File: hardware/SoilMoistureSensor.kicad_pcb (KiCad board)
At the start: 2 copper layers, 30 parts, among them Q1 AO3401A, SW1 SW_Push, SW2 SW_Push, U1 BQ25570, U2 ESP32-C3-WROOM-02, U3 TLC555xD

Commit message: started layout in pcb
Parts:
- moved R3 60.9 mm to (172.5, 86.5), turned to 180 degrees
- moved R4 59.0 mm to (170.5, 88.5), turned to 180 degrees
- moved R6 57.9 mm to (174.0, 83.5), turned to -90 degrees
- moved R5 57.6 mm to (168.5, 86.5)
- moved R7 56.0 mm to (172.0, 83.0), turned to 90 degrees
- moved R2 53.8 mm to (165.5, 87.0), turned to 90 degrees
- moved R1 51.8 mm to (163.5, 85.0), turned to 90 degrees
- moved Q1 47.1 mm to (106.9, 84.5)
- moved C9 46.3 mm to (97.0, 62.0), turned to -90 degrees
- moved C1 42.6 mm to (167.0, 55.0)
- moved R12 37.0 mm to (156.5, 78.5)
- moved SW1 34.1 mm to (102.3, 63.1)
- moved C2 33.1 mm to (168.0, 77.0)
- moved SW2 32.7 mm to (102.5, 72.0)
- moved C3 32.5 mm to (168.0, 79.0)
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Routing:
- net /VRDIV: track 0.00 -> 18.9 mm
- net /OK_PROG_N: track 0.00 -> 5.94 mm
- net /VBAT: track 0.00 -> 5.91 mm
- net /VOUT_SET_N: track 0.00 -> 5.09 mm
- net /VBAT_OV_N: track 0.00 -> 4.94 mm
- net /OK_HYST_N: track 0.00 -> 4.63 mm
- net /VSTOR: track 0.00 -> 3.92 mm
- net /VREF_SAMP: track 0.00 -> 3.09 mm
- net GND: track 0.00 -> 2.33 mm

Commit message: continued placing parts in layout
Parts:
- moved C2 39.4 mm to (129.2, 70.0)
- moved C3 39.4 mm to (129.2, 72.0)
- moved C4 39.4 mm to (123.7, 75.0)
- moved C5 39.4 mm to (130.2, 68.0)
- moved R1 39.4 mm to (124.7, 78.0)
- moved R2 39.4 mm to (126.7, 80.0)
- moved R3 39.4 mm to (133.7, 79.5)
- moved R4 39.4 mm to (131.7, 81.5)
- moved R5 39.4 mm to (129.7, 79.5)
- moved R6 39.4 mm to (135.2, 76.5)
- moved R7 39.4 mm to (133.2, 76.0)
- moved U1 39.4 mm to (129.0, 75.5)
- moved C6 39.1 mm to (161.0, 97.5)
- moved C7 39.1 mm to (161.0, 93.0)
- moved C8 39.1 mm to (161.0, 95.0)
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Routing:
- net +3V3: track 0.00 -> 94.0 mm
- net GND: track 2.33 -> 49.5 mm, vias 0 -> 7
- net /EN_ESP: track 0.00 -> 18.9 mm
- net /SENSOR_PWR_EN: track 0.00 -> 18.7 mm
- net /FREQ_IN: track 0.00 -> 16.1 mm
- net /VIN_DC: track 0.00 -> 15.5 mm
- net /RV1_WIPER_TIE: track 0.00 -> 8.86 mm
- net /VCC_SENSOR: track 0.00 -> 8.46 mm
- net /OSC_RC: track 0.00 -> 8.17 mm
- net /GPIO9_BOOT: track 0.00 -> 4.80 mm
- net /SENSOR_GATE: track 0.00 -> 4.64 mm
- net /OSC_RC_DISCH: track 0.00 -> 2.70 mm
- net /CTRL_BP: track 0.00 -> 1.92 mm
- added copper zone on B.Cu, net GND
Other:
- board outline added: 43 x 89.5 mm

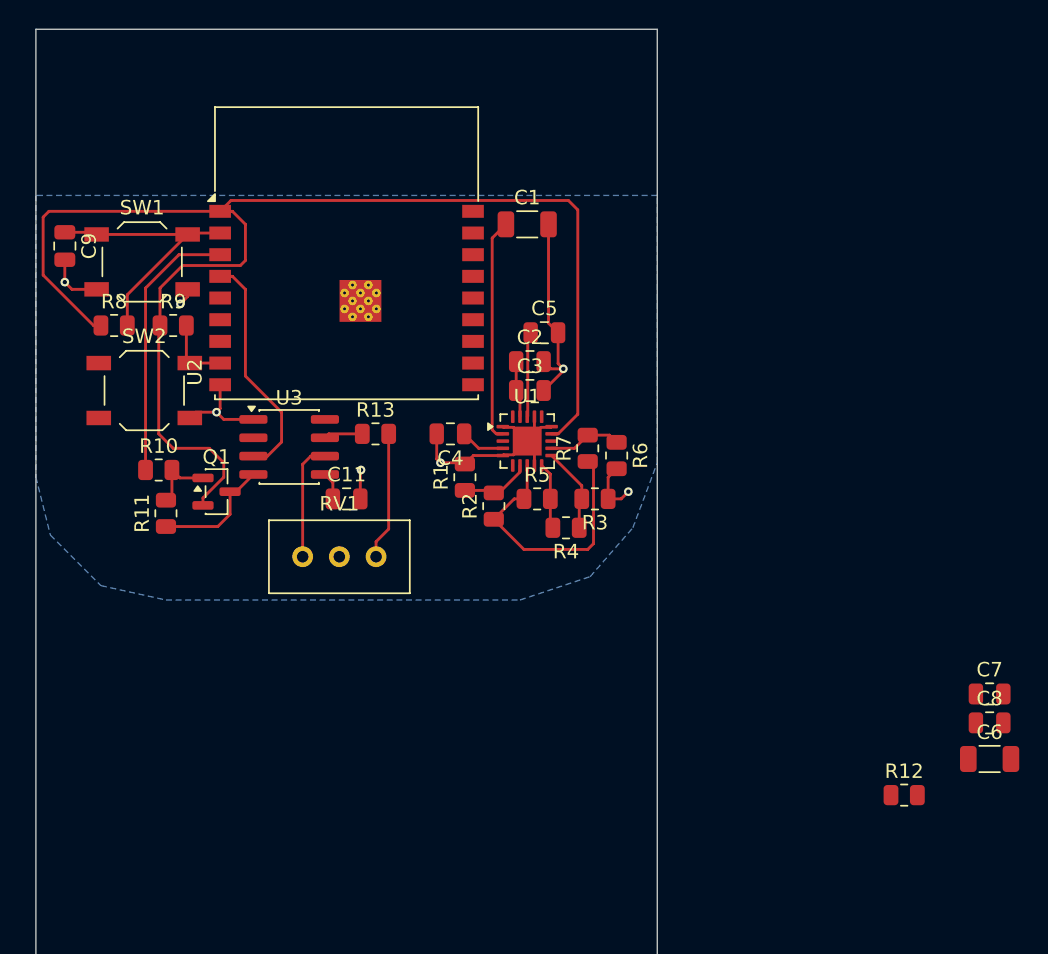
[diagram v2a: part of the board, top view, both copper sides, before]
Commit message: completed routing of board. still need to add capacitive sensing traces
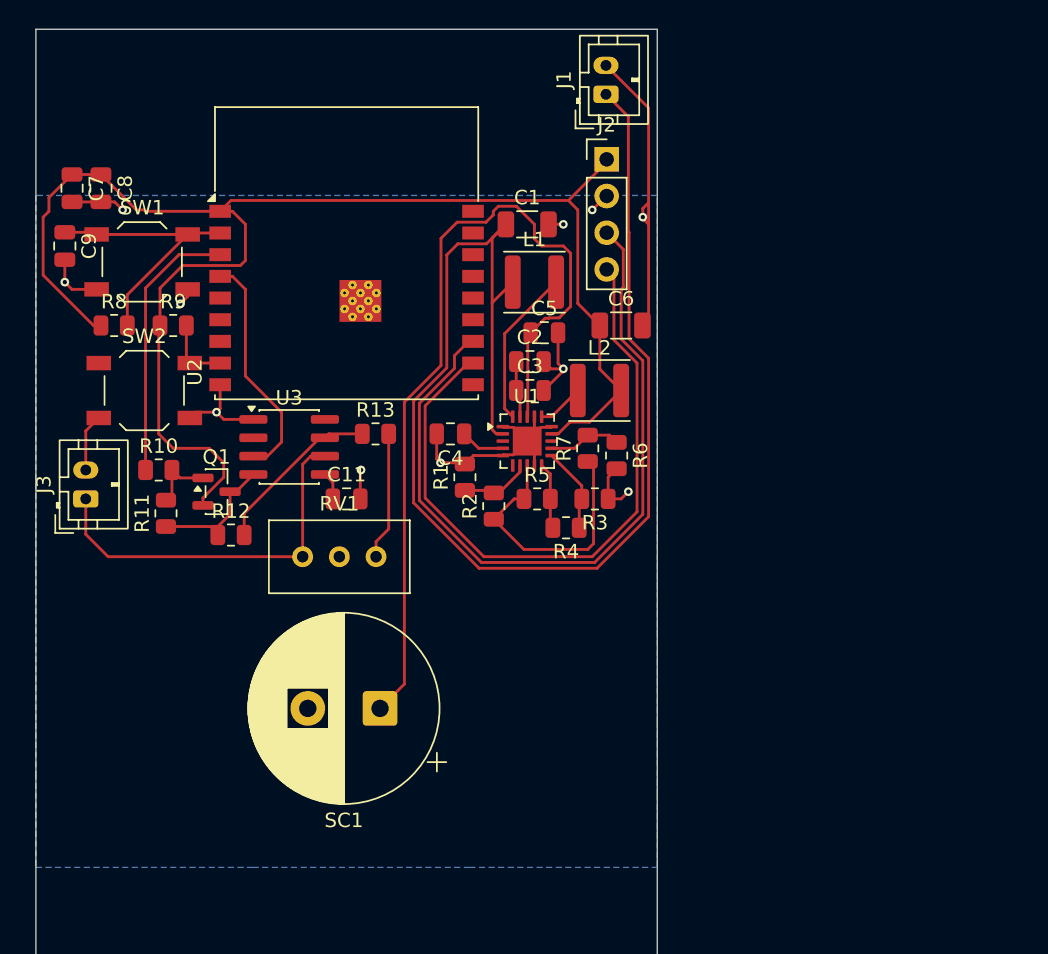
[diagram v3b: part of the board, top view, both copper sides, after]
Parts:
- added J1: Conn_01x02, Connector_JST:JST_PH_B2B-PH-K_1x02_P2.00mm_Vertical, F.Cu at (134.4, 51.5)
- added J2: Conn_01x04, Connector_PinHeader_2.54mm:PinHeader_1x04_P2.54mm_Vertical, F.Cu at (134.5, 56.0)
- added J3: Conn_01x02, Connector_JST:JST_PH_B2B-PH-K_1x02_P2.00mm_Vertical, F.Cu at (98.5, 79.5)
- added L1: 22uH, Inductor_SMD:L_APV_ANR4030, F.Cu at (129.5, 64.5)
- added L2: 10uH, Inductor_SMD:L_APV_ANR4030, F.Cu at (134.0, 72.0)
- added SC1: 3F 5.5V Supercap, Capacitor_THT:CP_Radial_D13.0mm_P5.00mm, F.Cu at (118.8, 94.0)
- moved C7 72.5 mm to (97.5, 58.0), turned to -90 degrees
- moved C8 71.8 mm to (99.5, 58.0), turned to -90 degrees
- moved R12 49.9 mm to (108.5, 82.0)
- moved C6 39.4 mm to (135.5, 67.5)
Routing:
- net /VIN_DC: track 15.5 -> 90.6 mm
- net /VBAT: track 5.91 -> 59.4 mm
- net /ESP_TXD: track 0.00 -> 52.0 mm
- net /ESP_RXD: track 0.00 -> 46.2 mm
- net GND: track 49.5 -> 73.1 mm, vias 7 -> 11
- net /OSC_RC: track 8.17 -> 26.3 mm
- net /LBOOST: track 0.00 -> 11.0 mm
- net +3V3: track 94.0 -> 104.0 mm
- net /OSC_RC_DISCH: track 2.70 -> 11.9 mm
- net /LBUCK: track 0.00 -> 3.25 mm

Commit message: astra redesigned then ran out of usage
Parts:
- removed R6: 4.75M 1%, Resistor_SMD:R_0805_2012Metric
- removed R7: 8.25M 1%, Resistor_SMD:R_0805_2012Metric
- added C10: 100nF 10V, Capacitor_SMD:C_0805_2012Metric, F.Cu at (118.0, 74.8)
- added C12: 10uF 10V X7R, Capacitor_SMD:C_0805_2012Metric, F.Cu at (134.5, 108.3)
- added J4: PCB capacitive probe, SoilProbe:SoilProbe_IDC_40x30mm, F.Cu at (116.5, 135.0)
- added R14: 10k, Resistor_SMD:R_0805_2012Metric, F.Cu at (104.0, 86.5)
- added R15: 10k, Resistor_SMD:R_0805_2012Metric, F.Cu at (129.0, 61.0)
- added R16: 52.3k 1%, Resistor_SMD:R_0805_2012Metric, F.Cu at (126.0, 111.5)
- added U4: TPS62842DGRR, Package_SO:HVSSOP-8-1EP_3x3mm_P0.65mm_EP1.57x1.89mm, F.Cu at (130.0, 108.0)
- C1, C2: value 4.7uF -> 4.7uF 10V X7R
- C11: value 100nF -> 10nF
- C3: value 0.1uF -> 100nF 10V
- C4: value 10nF -> 10nF C0G 5%
- C5, C8, C9: value 100nF -> 100nF 10V
- C6: value 22uF -> 10uF 10V X7R
- C7: value 10uF -> 10uF 10V X7R
- L1: value 22uH -> 22uH / Isat >= 0.4A; footprint Inductor_SMD:L_APV_ANR4030 -> Inductor_SMD:L_Coilcraft_LPS4018
- L2: value 10uH -> 2.2uH / Isat >= 1.5A; footprint Inductor_SMD:L_APV_ANR4030 -> Inductor_SMD:L_Coilcraft_LPS4018
- R1: value 3.01M 1% -> 4.75M 1%
- R12: value 1k -> 10k
- R13: value 4.7k -> 47k
- R2: value 10.0M 1% -> 8.25M 1%
- RV1: value 10k trim -> 100k trim
- SC1: value 3F 5.5V Supercap -> 3F 5.4V PHV-5R4V305-R; footprint Capacitor_THT:CP_Radial_D13.0mm_P5.00mm -> SoilProbe:CP_Eaton_PHV_3F_Vertical_P11.8mm
- moved C6 34.4 mm to (123.0, 99.5)
- moved L2 32.9 mm to (124.5, 103.5), turned to 180 degrees
- moved C1 23.0 mm to (124.0, 83.0)
- moved L1 23.0 mm to (124.5, 87.0)
- moved C2 16.2 mm to (131.5, 86.0)
- moved C3 16.0 mm to (129.2, 88.0)
- moved C4 16.0 mm to (123.7, 91.0)
- moved C5 16.0 mm to (130.2, 84.0)
- moved R1 16.0 mm to (124.7, 94.0)
- moved R2 16.0 mm to (126.7, 96.0)
- moved R3 16.0 mm to (133.7, 95.5)
- moved R4 16.0 mm to (131.7, 97.5)
- moved R5 16.0 mm to (129.7, 95.5)
- moved U1 16.0 mm to (129.0, 91.5)
- moved SC1 12.5 mm to (108.5, 101.0), turned to 0 degrees
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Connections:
- C1 pad 2: GND -> /GND
- C11 pad 2: GND -> /GND
- C2 pad 2: GND -> /GND
- C3 pad 2: GND -> /GND
- C4 pad 2: GND -> /GND
- C5 pad 2: GND -> /GND
- C6 pad 1: +3V3 -> /+3V3
- C6 pad 2: GND -> /GND
- C7 pad 1: +3V3 -> /+3V3
- C7 pad 2: GND -> /GND
- C8 pad 1: +3V3 -> /+3V3
- C8 pad 2: GND -> /GND
- C9 pad 2: GND -> /GND
- J1 pad 2: GND -> /GND
- J2 pad 1: +3V3 -> /+3V3
- J2 pad 2: GND -> /GND
- J3 pad 2: GND -> /GND
- L2 pad 1: /LBUCK -> /BUCK_SW
- L2 pad 2: +3V3 -> /+3V3
- Q1 pad 2: +3V3 -> /+3V3
- R1 pad 2: GND -> /GND
- R11 pad 1: /VCC_SENSOR -> /+3V3
- R3 pad 1: GND -> /GND
- R8 pad 1: +3V3 -> /+3V3
- R9 pad 1: +3V3 -> /+3V3
- SC1 pad 2: GND -> /GND
- SW1 pad 2: GND -> /GND
- SW2 pad 2: GND -> /GND
- U1 pad 1: GND -> /GND
- U1 pad 12: /VOUT_SET_N -> /GND
- U1 pad 14: +3V3 -> unconnected-(U1-VOUT-Pad14)
- U1 pad 15: GND -> /GND
- U1 pad 16: /LBUCK -> unconnected-(U1-LBUCK-Pad16)
- U1 pad 17: GND -> /GND
- U1 pad 21: GND -> /GND
- U1 pad 5: GND -> /GND
- U1 pad 6: /BAT_OK -> /GND
- U1 pad 9: GND -> /GND
- U2 pad 1: +3V3 -> /+3V3
- U2 pad 16: unconnected-(U2-IO2-Pad16) -> /GPIO2_BOOT
- U2 pad 19: GND -> /GND
- U2 pad 7: unconnected-(U2-IO8-Pad7) -> /GPIO8_BOOT
- U2 pad 9: GND -> /GND
- U3 pad 1: GND -> /GND
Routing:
- net /+3V3: track 0.00 -> 121.0 mm, vias 0 -> 12
- net +3V3: track 104.0 -> 0.00 mm
- net GND: track 73.1 -> 0.00 mm, vias 11 -> 0
- net /OSC_RC: track 26.3 -> 79.9 mm, vias 0 -> 2
- net /VIN_DC: track 90.6 -> 41.7 mm
- net /ESP_TXD: track 52.0 -> 12.4 mm
- net /ESP_RXD: track 46.2 -> 12.0 mm
- net /GPIO9_BOOT: track 4.80 -> 27.8 mm
- net /GPIO8_BOOT: track 0.00 -> 19.1 mm, vias 0 -> 2
- net /BAT_OK: track 0.00 -> 19.0 mm, vias 0 -> 2
- net /VCC_SENSOR: track 8.46 -> 27.3 mm, vias 0 -> 2
- net /VBAT: track 59.4 -> 44.0 mm
- net /GND: track 0.00 -> 10.4 mm, vias 0 -> 5
- net /OSC_RC_DISCH: track 11.9 -> 21.2 mm
- net /LBOOST: track 11.0 -> 3.61 mm, vias 0 -> 2
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- added copper zone on B.Cu, net /GND
- added copper zone on F.Cu, net /GND
- removed copper zone on B.Cu, net GND
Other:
- board size 43 x 89.5 mm -> 43 x 104.5 mm
- board text added: "3V3 OUT"
- board text added: "RX TX GND"
- board text added: "SOIL LINE - SEAL BELOW"
- board text added: "SOIL MOISTURE / REV B"
- board text added: "SOLAR + / -"

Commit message: told astra to lengthen board, choose solar panel, and keep all parts jlcpcb basic
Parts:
- added R17: 2M 1%, Resistor_SMD:R_0603_1608Metric, F.Cu at (115.0, 93.5)
- added R18: 2M 1%, Resistor_SMD:R_0603_1608Metric, F.Cu at (111.5, 88.5)
- added R19: 3M 1%, Resistor_SMD:R_0603_1608Metric, F.Cu at (108.0, 88.5)
- added R20: 2M 1%, Resistor_SMD:R_0603_1608Metric, F.Cu at (108.0, 93.5)
- added R21: 2M 1%, Resistor_SMD:R_0603_1608Metric, F.Cu at (104.5, 91.0)
- added R22: 2M 1%, Resistor_SMD:R_0603_1608Metric, F.Cu at (101.0, 91.0)
- added R23: 2M 1%, Resistor_SMD:R_0603_1608Metric, F.Cu at (101.0, 93.5)
- C1: value 4.7uF 10V X7R -> 4.7uF 25V X5R; footprint Capacitor_SMD:C_1206_3216Metric -> Capacitor_SMD:C_0805_2012Metric
- C10, C3, C5, C8, C9: value 100nF 10V -> 100nF 50V X7R
- C11: value 10nF -> 10nF 50V X7R
- C12, C7: value 10uF 10V X7R -> 10uF 25V X5R
- C2: value 4.7uF 10V X7R -> 4.7uF 25V X5R
- C6: value 10uF 10V X7R -> 10uF 25V X5R; footprint Capacitor_SMD:C_1206_3216Metric -> Capacitor_SMD:C_0805_2012Metric
- J4: footprint SoilProbe:SoilProbe_IDC_40x30mm -> SoilProbe:SoilProbe_IDC_40x55mm
- R1: value 4.75M 1% -> 2M 1%; footprint Resistor_SMD:R_0805_2012Metric -> Resistor_SMD:R_0603_1608Metric
- R2: value 8.25M 1% -> 2M 1%; footprint Resistor_SMD:R_0805_2012Metric -> Resistor_SMD:R_0603_1608Metric
- R3: value 2.49M 1% -> 2M 1%; footprint Resistor_SMD:R_0805_2012Metric -> Resistor_SMD:R_0603_1608Metric
- R4: value 4.99M 1% -> 2M 1%; footprint Resistor_SMD:R_0805_2012Metric -> Resistor_SMD:R_0603_1608Metric
- R5: value 866k 1% -> 1.5M 1%; footprint Resistor_SMD:R_0805_2012Metric -> Resistor_SMD:R_0603_1608Metric
- SW1, SW2: value SW_Push -> TS-1088-AR02016; footprint Button_Switch_SMD:SW_SPST_TL3342 -> Button_Switch_SMD:SW_SPST_TS-1088-xR020
- U2: value ESP32-C3-WROOM-02 -> ESP32-C3-WROOM-02-N4; footprint RF_Module:ESP32-C3-WROOM-02 -> SoilProbe:ESP32-C3-WROOM-02_0.3mm_thermal_vias
- U3: value TLC555xD -> TLC555CDR
- moved C10 50.3 mm to (115.5, 125.0)
- moved C11 49.4 mm to (110.0, 128.5)
- moved U3 48.2 mm to (110.0, 124.0)
- moved R13 46.2 mm to (117.0, 121.0)
- moved R12 39.7 mm to (101.0, 121.0)
- moved J3 35.5 mm to (99.0, 115.0), turned to 0 degrees
- moved RV1 33.1 mm to (116.5, 116.5)
- moved R5 29.5 mm to (101.0, 88.5)
- moved R3 29.3 mm to (104.5, 93.5), turned to 0 degrees
- moved J4 27.5 mm to (116.5, 162.5)
- moved R4 24.6 mm to (108.0, 91.0), turned to 0 degrees
- moved R2 13.9 mm to (115.0, 88.5), turned to 0 degrees
- moved R1 10.1 mm to (115.0, 91.0), turned to 0 degrees
- moved C3 4.43 mm to (133.5, 89.0)
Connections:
- R1 pad 2: /GND -> /OV_LO_SER
- R2 pad 2: /VBAT_OV_N -> /OV_HI_SER1
- R3 pad 2: /OK_PROG_N -> /OK_LO_SER
- R4 pad 2: /OK_HYST_N -> /OK_MID_SER1
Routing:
- net /FREQ_IN: track 16.1 -> 75.9 mm, vias 0 -> 4
- net /VCC_SENSOR: track 27.3 -> 77.2 mm, vias 2 -> 0
- net /OK_PROG_N: track 5.94 -> 43.0 mm, vias 0 -> 4
- net /OK_HYST_N: track 4.63 -> 38.1 mm, vias 0 -> 2
- net /VBAT: track 44.0 -> 67.9 mm, vias 0 -> 3
- net /OSC_RC: track 79.9 -> 57.5 mm, vias 2 -> 1
- net /GND: track 10.4 -> 32.7 mm, vias 5 -> 15
- net /VBAT_OV_N: track 4.94 -> 25.4 mm, vias 0 -> 2
- net /VRDIV: track 18.9 -> 36.0 mm, vias 0 -> 6
- net /VIN_DC: track 41.7 -> 53.0 mm, vias 0 -> 2
- net /OK_MID_SER2: track 0.00 -> 9.81 mm
- net /GPIO9_BOOT: track 27.8 -> 35.9 mm
- net /VSTOR: track 10.7 -> 16.7 mm
- net /OV_HI_SER2: track 0.00 -> 5.95 mm
- net /OV_HI_SER1: track 0.00 -> 5.95 mm
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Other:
- board size 43 x 104.5 mm -> 43 x 144.5 mm
- board text added: "+"
- board text added: "-"
- board text added: "3V3"
- board text added: "GND"
- board text added: "MAX SOIL LINE / SEAL BELOW"
- board text added: "RX"
- board text added: "SOLAR"
- board text added: "TX"
- board text removed: "3V3 OUT"
- board text removed: "RX TX GND"
- board text removed: "SOIL LINE - SEAL BELOW"
- board text removed: "SOLAR + / -"

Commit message: had claude go in and fix what astra didnt finish. extended length to 3.5inch
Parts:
- J4: footprint SoilProbe:SoilProbe_IDC_40x55mm -> SoilProbe:SoilProbe_IDC_40x85mm
- moved J4 15.0 mm to (116.5, 177.5)
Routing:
- net /GND: track 32.7 -> 31.0 mm
- net /FREQ_IN: track 75.9 -> 74.4 mm
- net /VCC_SENSOR: track 77.2 -> 77.9 mm
- net /OSC_RC: track 57.5 -> 58.2 mm
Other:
- board size 43 x 144.5 mm -> 43 x 174.5 mm
- board text added: "1 in"
- board text added: "2 in"
- board text added: "3 in"
- board text added: "3.5 in"
